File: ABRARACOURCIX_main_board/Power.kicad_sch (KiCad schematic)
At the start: 29 parts, among them J3 XT60PW-M, Q2 NTR4101PT1G, SW1 Motor, SW2 Master, U2 Current_sens_ACS712ELCTR-20A-T, U3 AZ1117CH-3.3TRG1, U4 Xl4015, U6 LMC6482, U7 LMC6482

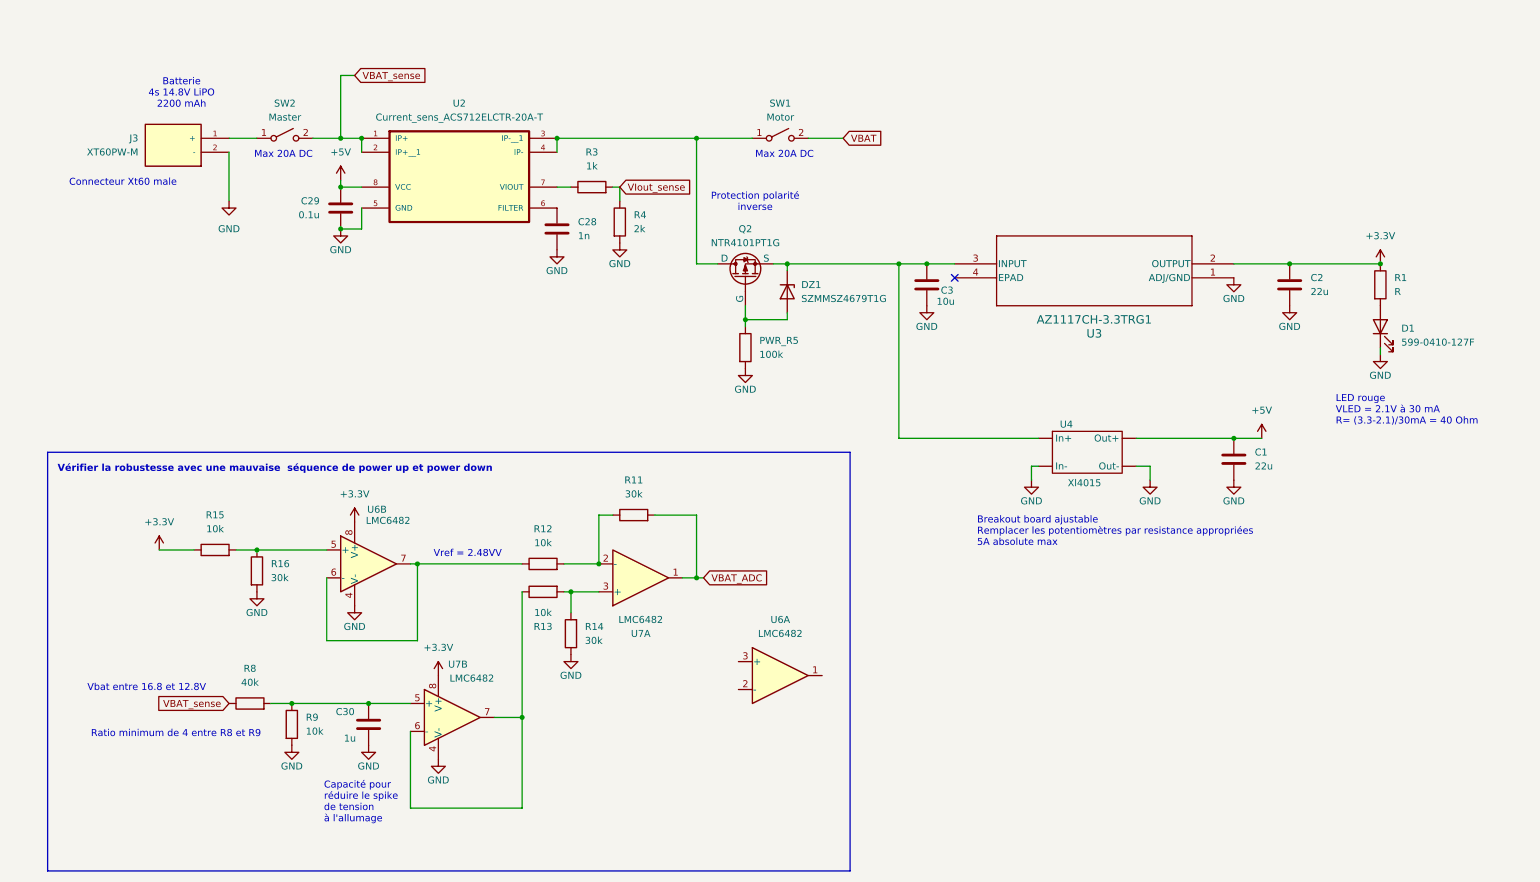
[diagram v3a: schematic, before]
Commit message: Assignation d<empreintes terminée
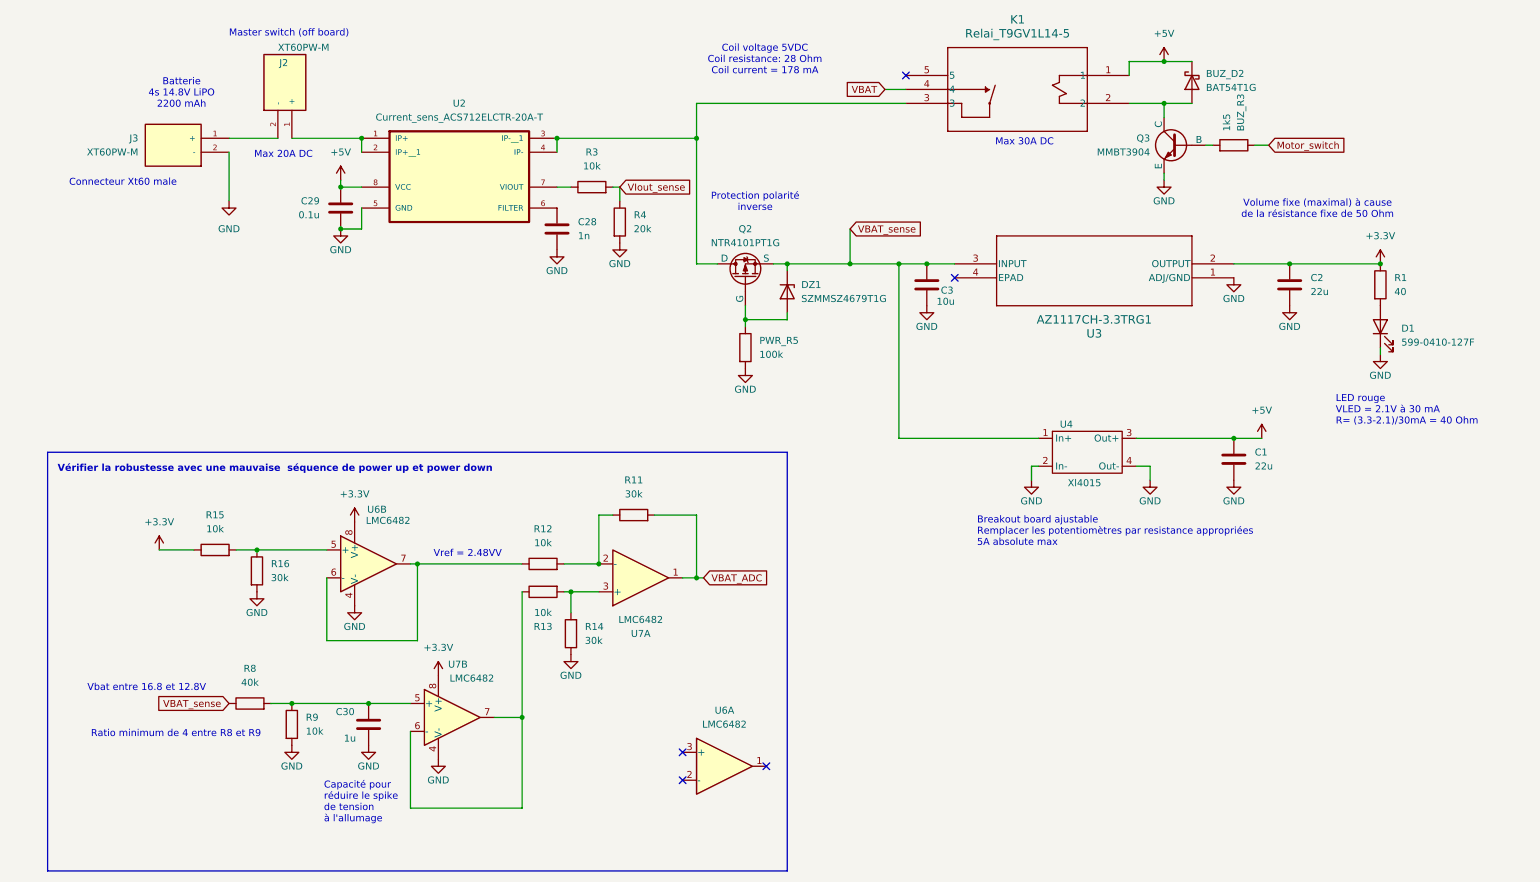
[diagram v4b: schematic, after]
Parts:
- removed SW1: Motor, symbol Switch:SW_SPST
- removed SW2: Master, symbol Switch:SW_SPST
- added BUZ_D2: BAT54T1G, Diode_SMD:D_SOD-123, symbol Diode:1N6858UR
- added BUZ_R3: 1k5, Resistor_SMD:R_1206_3216Metric_Pad1.30x1.75mm_HandSolder, symbol Device:R
- added J2: XT60PW-M, Connector_AMASS:AMASS_XT60-F_1x02_P7.20mm_Vertical, symbol GAUL_ABRARACOURCIX:XT60PW-M
- added K1: Relai_T9GV1L14-5, Librairie_footprint:Relai_30A_T9GV1L14-5_TEC, symbol GAUL_ABRARACOURCIX:Relai_T9GV1L14-5
- added Q3: MMBT3904, Package_TO_SOT_SMD:SOT-23-3, symbol Simulation_SPICE:NPN
- C1: footprint (none) -> Resistor_SMD:R_0805_2012Metric
- C2, C28, C29, C3, C30: footprint (none) -> Capacitor_SMD:C_1206_3216Metric_Pad1.33x1.80mm_HandSolder
- D1: footprint (none) -> Diode_SMD:D_1206_3216Metric_Pad1.42x1.75mm_HandSolder
- J3: footprint XT60PW-M:AMASS_XT60PW-M -> Librairie_footprint:AMASS_XT60PW-M
- PWR_R5: footprint Resistor_SMD:R_1206_3216Metric -> Resistor_SMD:R_1206_3216Metric_Pad1.30x1.75mm_HandSolder
- Q2: footprint Footprints:SOT-23 -> Package_TO_SOT_SMD:SOT-23-3
- R1: value R -> 40; footprint (none) -> Resistor_SMD:R_1206_3216Metric_Pad1.30x1.75mm_HandSolder
- R11, R12, R13, R14, R15, R16, R8, R9: footprint (none) -> Resistor_SMD:R_1206_3216Metric_Pad1.30x1.75mm_HandSolder
- R3: value 1k -> 10k; footprint (none) -> Resistor_SMD:R_1206_3216Metric_Pad1.30x1.75mm_HandSolder
- R4: value 2k -> 20k; footprint (none) -> Resistor_SMD:R_1206_3216Metric_Pad1.30x1.75mm_HandSolder
- U2: footprint ACS712ELCTR-20A-T:SOIC127P600X175-8N -> Librairie_footprint:Current_sens_SOIC127P600X175-8N
- U3: footprint SOT-223_DIO -> Librairie_footprint:AZ1117CH_3_3TRG1-L
- U4: footprint (none) -> Librairie_footprint:Buck_breakout_Xl4015
- U6, U7: footprint (none) -> Librairie_footprint:SOIC127P599X175-8N
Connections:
- net +5V: now also U4.3 (Out+), BUZ_D2.1 (K), K1.1; no longer U4. (Out-)
- net GND: now also U4.2 (In-), U4.4 (Out-), Q3.3 (E); no longer U4. (Out-)
- net VBAT: now also K1.4
- net VBAT_sense: now also C3.1, DZ1.1 (K), Q2.3 (S), U3.3 (INPUT), U4.1 (In+); no longer U2.1 (IP+), U2.2 (IP+__1)
- net at J3.1 (+): now also J2.2 (-)
- net at Q2.1 (D), U2.3 (IP-__1), U2.4 (IP-): now also K1.3
- new net: BUZ_R3.2, Q3.2 (B)
- new net: J2.1 (+), U2.1 (IP+), U2.2 (IP+__1)
- new net: BUZ_D2.2 (A), K1.2, Q3.1 (C)
- new net Motor_switch: BUZ_R3.1
- no-connect marks 1 -> 5
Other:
- note added: "Coil voltage 5VDC Coil resistance: 28 Ohm Coil current = 178 mA"
- note added: "Master switch (off board)"
- note added: "Max 30A DC"
- note added: "Volume fixe (maximal) à cause de la résistance fixe de 50 Ohm"
- moved on the sheet: U6A
